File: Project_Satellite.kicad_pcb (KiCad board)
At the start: 4 copper layers, 63.8 x 61 mm, 76 parts, among them J1 Conn_01x02_Socket, J2 Conn_01x02_Socket, J25 Conn_01x03_Socket, J26 Conn_01x03_Socket, J3 Conn_01x02_Socket, J4 Conn_01x02_Socket, U3 TPS62933, U4 RASPBERRY_PI_ZERO_2_W, U5 TLV320AIC3254IRHBR, U8 TPA3118D2DAPR

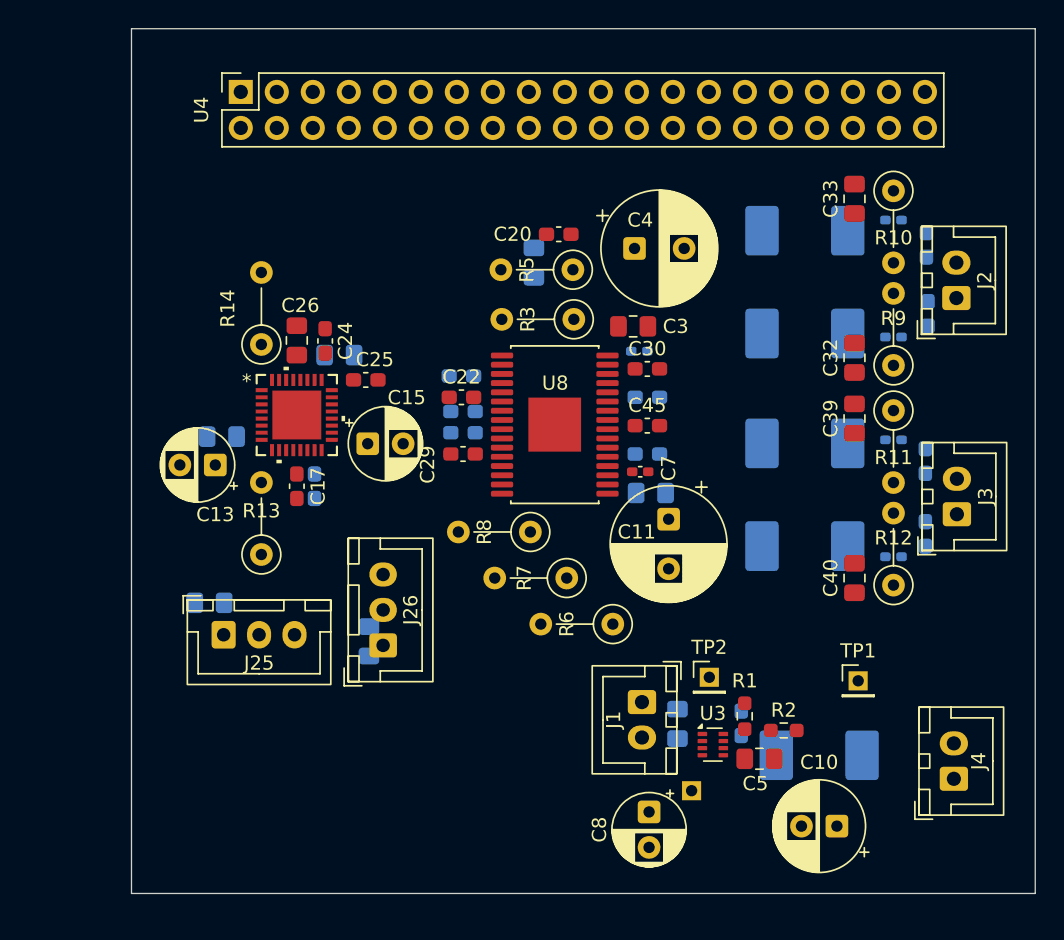
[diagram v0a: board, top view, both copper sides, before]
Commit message: Fully routed PCB V2 with Mic boards
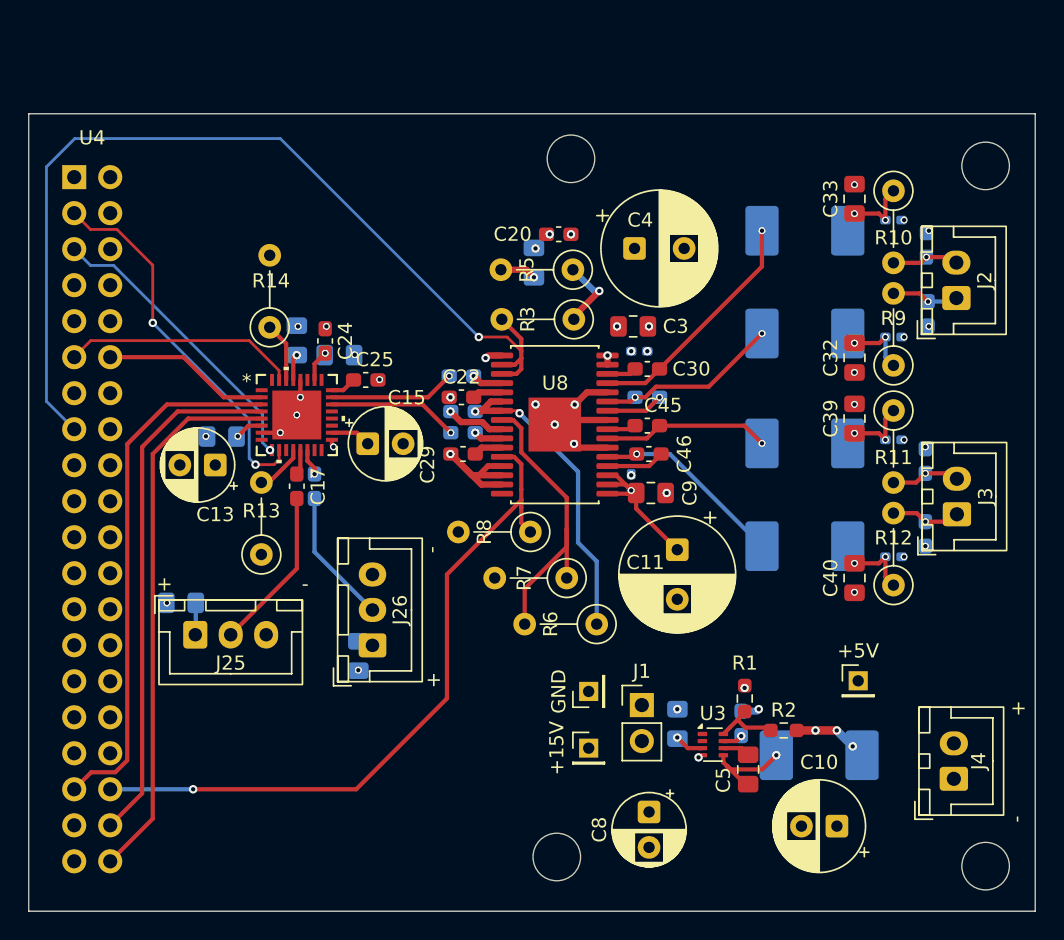
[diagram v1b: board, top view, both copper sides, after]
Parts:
- +15V: renamed from TP3; moved to F.Cu
- C26, C7, U4: moved to B.Cu
- C46, C9: moved to F.Cu
- J1: footprint Connector_JST:JST_XH_B2B-XH-A_1x02_P2.50mm_Vertical -> Connector_PinHeader_2.54mm:PinHeader_1x02_P2.54mm_Vertical
- moved U4 13.2 mm to (34.7, 103.5), turned to 180 degrees
- moved GND 8.57 mm to (71.0, 139.8), turned to 90 degrees
- moved +15V 7.86 mm to (71.0, 143.8), turned to 0 degrees
- moved C11 2.24 mm to (77.2, 129.8)
- moved C47 2.00 mm to (42.2, 133.5)
- moved J25 2.00 mm to (43.2, 135.8)
- moved R14 1.35 mm to (48.5, 114.1)
- moved C16 1.28 mm to (54.8, 137.2)
- moved R1 1.25 mm to (82.0, 140.2)
- moved R6 1.14 mm to (71.6, 135.0)
- moved C5 1.09 mm to (82.2, 145.2), turned to -90 degrees
- moved C7 0.98 mm to (74.0, 125.0), turned to 90 degrees
- moved J26 0.75 mm to (55.8, 136.5)
- moved J1 0.21 mm to (74.8, 140.7), turned to 0 degrees
- moved C46 0.11 mm to (75.2, 123.0)
- renumbered TP1 to +5V, TP2 to GND
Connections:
- U4 pad 11: /SDZ -> /RESET
- U4 pad 15: /MUTE -> /SDZ
- U4 pad 36: /RESET -> /MUTE
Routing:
- net /SDZ: track 0.00 -> 67.0 mm, vias 0 -> 1
- net /MUTE: track 0.00 -> 49.2 mm, vias 0 -> 1
- net GND: track 0.00 -> 42.8 mm, vias 0 -> 39
- net Net-(U4-GPIO21): track 0.00 -> 38.7 mm
- net Net-(U4-GPIO19): track 0.00 -> 37.5 mm
- net Net-(U4-GPIO20): track 0.00 -> 37.1 mm
- net /SDA: track 0.00 -> 26.6 mm, vias 0 -> 2
- net Net-(U8-GVDD): track 0.00 -> 22.5 mm, vias 0 -> 2
- net Net-(U8-GAIN/SLV): track 0.00 -> 21.5 mm
- net /SCL: track 0.00 -> 21.0 mm, vias 0 -> 1
- net Net-(U8-OUTPR): track 0.00 -> 16.8 mm, vias 0 -> 1
- net /RESET: track 0.00 -> 16.5 mm
- net Net-(U8-OUTNL): track 0.00 -> 13.7 mm, vias 0 -> 1
- net Net-(U8-OUTNR): track 0.00 -> 12.9 mm, vias 0 -> 2
- net Net-(U4-GPIO18/GPIO_GEN1): track 0.00 -> 11.9 mm
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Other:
- board size 63.8 x 61 mm -> 71 x 56.2 mm
- board text added: "+"
- board text added: "-"
